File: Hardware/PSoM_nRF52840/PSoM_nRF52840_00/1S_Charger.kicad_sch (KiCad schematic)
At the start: 12 parts, among them U2 NPM1300-QEAA-R

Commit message: working on nrf52840
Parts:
- removed D201, D202: LED, LED_SMD:LED_0402_1005Metric, symbol Component_lib:LED
- removed R205, R206: 1k5, Resistor_SMD:R_0402_1005Metric, symbol Component_lib:R
- added C201, C205: 1u, symbol Component_lib:C
- added C202, C203, C204: 10u, symbol Component_lib:C
- added C206: 2u2, symbol Component_lib:C
- C207: renamed from C2; value C -> 10u
- C208: renamed from C3; value C -> 10u
- L201: renamed from L3; value L -> 2u2
- L202: renamed from L4; value L -> 2u2
- R203: renamed from R2; value 0 -> 47k
- renumbered R1 to R204, SHIPHLD to SHIPHLD1, U2 to U201
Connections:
- net BATTERY_TEMP: now also U201.18 (NTC)
- net GND: now also C207.2, C208.2, U201.2 (PVSS1), U201.28 (LSIN1/VINLDO1), U201.29 (LSOUT1/VOUTLDO1), U201.30 (LSIN2/VINLDO2), U201.31 (LSOUT2/VOUTLDO2), U201.6 (PVSS2), C201.1, C202.2, C203.2, C204.2, C205.2, C206.2
- net VBAT: now also U201.19 (VBAT), C206.1
- net VBUS: now also U201.21 (VBUS), C201.2
- net VSYS: now also U201.20 (VSYS), U201.4 (PVDD), C202.1, C203.1, C204.1
- net 3V3_EXT: now reaches L202.1
- net 3V3_EXT: now also C208.1, U201.32 (VOUT2)
- net SW2: now reaches L202.2
- net SW2: now also U201.5 (SW2)
- net 3V3_nRF: now reaches L201.1
- net 3V3_nRF: now also C207.1, U201.1 (VOUT1), U201.12 (VDDIO)
- net SW1: now reaches L201.2
- net SW1: now also U201.3 (SW1)
- net VBUS_OUT: now reaches U201.22 (VBUSOUT)
- net VBUS_OUT: now also C205.1
- net CC1: now reaches U201.23 (CC1)
- net CC2: now reaches U201.24 (CC2)
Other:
- note added: "200-1S Charger"
- note added: "VOUT1"
- note added: "VOUT2"
- note removed: "200- 1S Charger"
- moved on the sheet: C207, C208, L201, L202, R203, R204, SHIPHLD1, U201

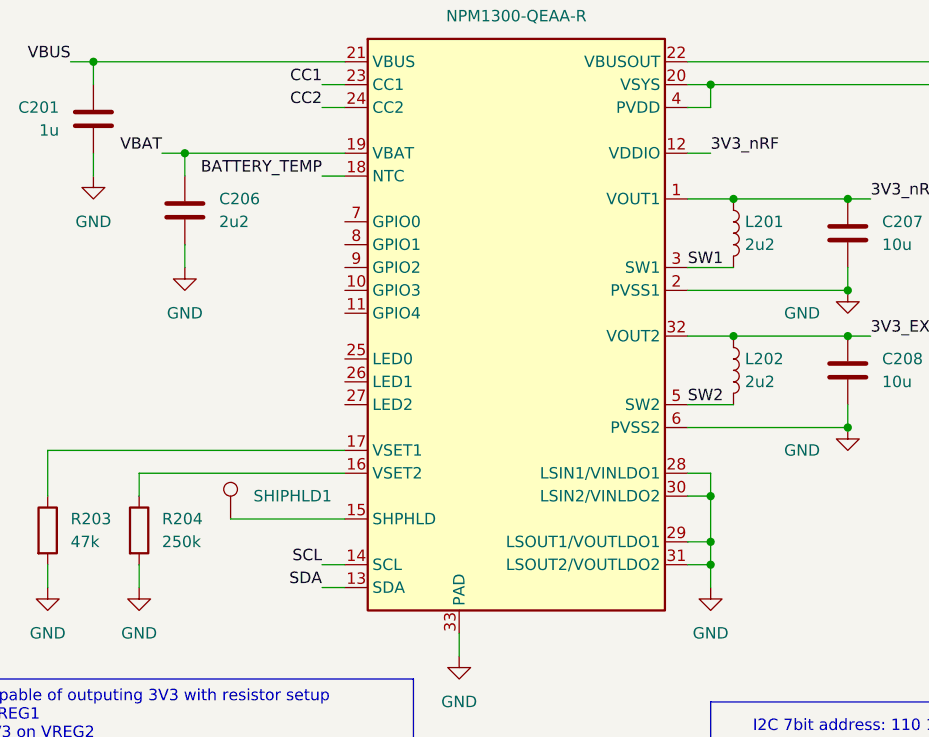
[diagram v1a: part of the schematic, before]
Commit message: footprint assignement done
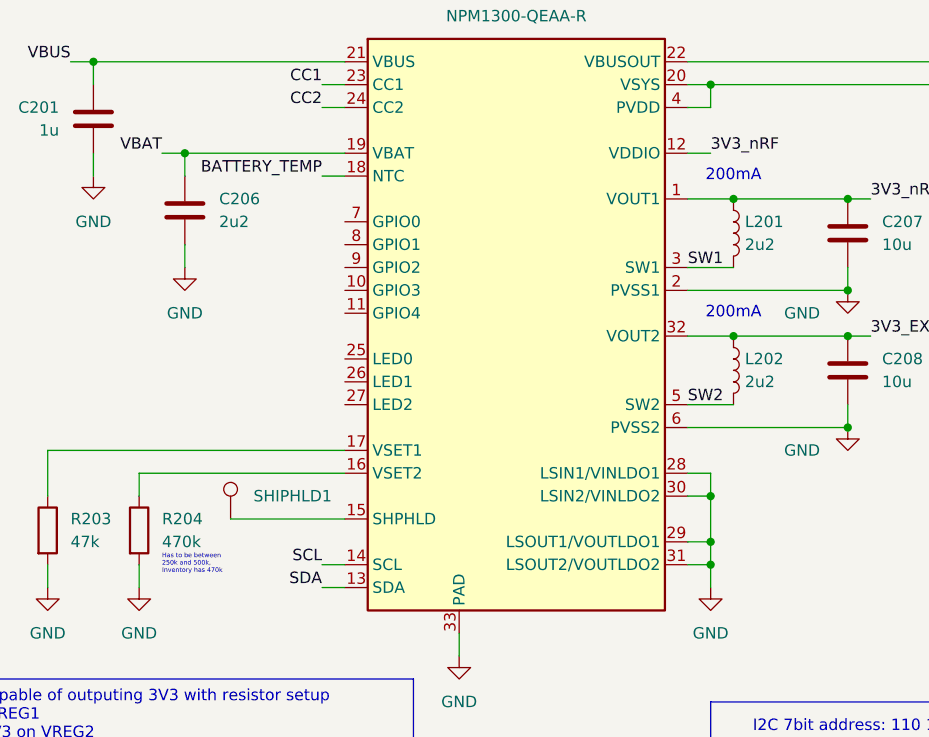
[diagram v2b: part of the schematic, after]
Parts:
- C201, C205, C207: footprint (none) -> Capacitor_SMD:C_0402_1005Metric
- C202, C203, C204, C206: footprint (none) -> Capacitor_SMD:C_0603_1608Metric
- C208: footprint (none) -> Capacitor_SMD:C_0402_1005Metric_Pad0.74x0.62mm_HandSolder
- L201, L202: footprint (none) -> Inductor_SMD:L_0603_1608Metric
- R203: footprint (none) -> Resistor_SMD:R_0201_0603Metric
- R204: value 250k -> 470k; footprint (none) -> Resistor_SMD:R_0201_0603Metric
- SHIPHLD1: footprint (none) -> TestPoint:TestPoint_Pad_D1.0mm
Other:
- note added: "200mA"
- note added: "Has to be between 250k and 500k, Inventory has 470k"
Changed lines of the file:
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@@
+		)
+	)
+	(text "200mA"
+		(exclude_from_sim no)
+		(at 167.64 81.28 0)
+		(effects
+			(font
+				(size 1.27 1.27)
+			)
+		)
+	)
+	(text "Has to be between\n250k and 500k,\nInventory has 470k"
+		(exclude_from_sim no)
+		(at 104.14 124.46 0)
+		(effects
+			(font
+				(size 0.508 0.508)
+			)
+			(justify left)
 		)
 	)
@@
 			(font
 				(face "Roboto")
+				(size 1.27 1.27)
+			)
+		)
+	)
+	(text "200mA"
+		(exclude_from_sim no)
+		(at 167.64 96.52 0)
+		(effects
+			(font
 				(size 1.27 1.27)
 			)
@@
 			)
 		)
-		(property "Footprint" ""
+		(property "Footprint" "Inductor_SMD:L_0603_1608Metric"
 			(at 167.64 102.87 90)
 			(effects
@@
 			)
 		)
-		(property "Footprint" ""
+		(property "Footprint" "Capacitor_SMD:C_0603_1608Metric"
 			(at 221.9452 81.28 0)
 			(effects
@@
 			)
 		)
-		(property "Footprint" ""
+		(property "Footprint" "Capacitor_SMD:C_0603_1608Metric"
 			(at 107.6452 88.9 0)
 			(effects
@@
 			)
 		)
-		(property "Footprint" ""
+		(property "Footprint" "Inductor_SMD:L_0603_1608Metric"
 			(at 167.64 87.63 90)
 			(effects
@@
 			)
 		)
-		(property "Footprint" ""
+		(property "Footprint" "Capacitor_SMD:C_0402_1005Metric"
 			(at 97.4852 71.12 0)
 			(effects
@@
 			)
 		)
-		(property "Footprint" ""
+		(property "Footprint" "Capacitor_SMD:C_0603_1608Metric"
 			(at 209.2452 81.28 0)
 			(effects
@@
 			)
 		)
-		(property "Footprint" ""
+		(property "Footprint" "TestPoint:TestPoint_Pad_D1.0mm"
 			(at 116.84 119.38 0)
 			(effects
@@
 			)
 		)
-		(property "Footprint" ""
+		(property "Footprint" "Resistor_SMD:R_0201_0603Metric"
 			(at 89.662 120.65 90)
 			(effects
@@
 			)
 		)
-		(property "Value" "250k"
+		(property "Value" "470k"
 			(at 104.14 121.9199 0)
 			(effects
@@
 			)
 		)
-		(property "Footprint" ""
+		(property "Footprint" "Resistor_SMD:R_0201_0603Metric"
 			(at 99.822 120.65 90)
 			(effects
@@
 			)
 		)
-		(property "Footprint" ""
+		(property "Footprint" "Capacitor_SMD:C_0402_1005Metric_Pad0.74x0.62mm_HandSolder"
 			(at 181.3052 106.68 0)
 			(effects
@@
 			)
 		)
-		(property "Footprint" ""
+		(property "Footprint" "Capacitor_SMD:C_0402_1005Metric"
 			(at 181.3052 91.44 0)
 			(effects
@@
 			)
 		)
-		(property "Footprint" ""
+		(property "Footprint" "Capacitor_SMD:C_0402_1005Metric"
 			(at 234.6452 78.74 0)
 			(effects
@@
 			)
 		)
-		(property "Footprint" ""
+		(property "Footprint" "Capacitor_SMD:C_0603_1608Metric"
 			(at 196.5452 81.28 0)
 			(effects

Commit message: working on schematic
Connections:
- net SHIP: now reaches SHIPHLD1.1, U201.15 (SHPHLD)
- net VSET2: now reaches R204.1, U201.16 (VSET2)
- net VSET1: now reaches R203.1, U201.17 (VSET1)
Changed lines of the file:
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@@
+		)
+	)
+	(label "VSET1"
+		(at 106.68 111.76 0)
+		(fields_autoplaced yes)
+		(effects
+			(font
+				(size 1.27 1.27)
+			)
+			(justify left bottom)
 		)
 	)
@@
 		)
 	)
+	(label "VSET2"
+		(at 106.68 114.3 0)
+		(fields_autoplaced yes)
+		(effects
+			(font
+				(size 1.27 1.27)
+			)
+			(justify left bottom)
+		)
+	)
 	(label "SCL"
 		(at 121.92 124.46 180)
@@
 		)
 	)
+	(label "SHIP"
+		(at 114.3 119.38 0)
+		(fields_autoplaced yes)
+		(effects
+			(font
+				(size 1.27 1.27)
+			)
+			(justify left bottom)
+		)
+	)

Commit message: routing is doing great progress
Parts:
- added D201, D202, D203: LED, symbol Component_lib:LED
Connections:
- net VSYS: now also D201.1 (A), D202.1 (A), D203.1 (A)
- net LED0: now reaches U201.25 (LED0)
- net LED0: now also D201.2 (K)
- net LED1: now reaches U201.26 (LED1)
- net LED1: now also D202.2 (K)
- net LED2: now reaches U201.27 (LED2)
- net LED2: now also D203.2 (K)
- no-connect marks 0 -> 5

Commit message: schematic should be done
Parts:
- D201, D202, D203: footprint (none) -> LED_SMD:LED_0402_1005Metric
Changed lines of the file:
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@@
+	(wire
+		(pts
+			(xy 266.7 73.66) (xy 269.24 73.66)
+		)
+		(stroke
+			(width 0)
+			(type default)
+		)
+	)
 	(wire
 		(pts
@@
 	(wire
 		(pts
-			(xy 269.24 68.58) (xy 266.7 68.58)
+			(xy 269.24 78.74) (xy 266.7 78.74)
 		)
 		(stroke
@@
 	(wire
 		(pts
-			(xy 266.7 68.58) (xy 266.7 71.12)
+			(xy 266.7 78.74) (xy 266.7 81.28)
 		)
 		(stroke
@@
 		(pts
 			(xy 55.88 86.36) (xy 55.88 88.9)
+		)
+		(stroke
+			(width 0)
+			(type default)
+		)
+	)
+	(wire
+		(pts
+			(xy 266.7 68.58) (xy 269.24 68.58)
 		)
 		(stroke
@@
 	(label "CC2"
 		(at 121.92 73.66 180)
+		(fields_autoplaced yes)
 		(effects
 			(font
@@
 	(label "VBAT"
 		(at 104.14 78.74 180)
+		(fields_autoplaced yes)
+		(effects
+			(font
+				(size 1.27 1.27)
+			)
+			(justify right bottom)
+		)
+	)
+	(label "SDA"
+		(at 266.7 73.66 180)
+		(fields_autoplaced yes)
 		(effects
 			(font
@@
 	(label "VSET1"
 		(at 106.68 111.76 0)
+		(fields_autoplaced yes)
 		(effects
 			(font
@@
 	(label "VBUS"
 		(at 93.98 68.58 180)
+		(fields_autoplaced yes)
 		(effects
 			(font
@@
 	(label "CC1"
 		(at 266.7 58.42 180)
+		(fields_autoplaced yes)
 		(effects
 			(font
@@
 	(label "CC2"
 		(at 266.7 63.5 180)
+		(fields_autoplaced yes)
 		(effects
 			(font
@@
 	(label "VBUS"
 		(at 266.7 27.94 180)
+		(fields_autoplaced yes)
 		(effects
 			(font
@@
 	(label "LED2"
 		(at 76.2 99.06 270)
+		(fields_autoplaced yes)
 		(effects
 			(font
@@
 	(label "BATTERY_TEMP"
 		(at 121.92 81.28 180)
+		(fields_autoplaced yes)
 		(effects
 			(font
@@
 	(label "VSYS"
 		(at 223.52 71.12 0)
+		(fields_autoplaced yes)
 		(effects
 			(font
@@
 	(label "VBUS_OUT"
 		(at 266.7 33.02 180)
+		(fields_autoplaced yes)
 		(effects
 			(font
@@
 	(label "LED1"
 		(at 66.04 99.06 270)
+		(fields_autoplaced yes)
 		(effects
 			(font
@@
 	(label "LED2"
 		(at 121.92 106.68 180)
+		(fields_autoplaced yes)
 		(effects
 			(font
@@
 	(label "LED0"
 		(at 121.92 101.6 180)
+		(fields_autoplaced yes)
 		(effects
 			(font
@@
 	(label "LED0"
 		(at 55.88 99.06 270)
+		(fields_autoplaced yes)
 		(effects
 			(font
@@
 	(label "3V3_nRF"
 		(at 182.88 83.82 0)
+		(fields_autoplaced yes)
 		(effects
 			(font
@@
 	(label "VBUS_OUT"
 		(at 236.22 68.58 0)
+		(fields_autoplaced yes)
 		(effects
 			(font
@@
 	(label "BATTERY_TEMP"
 		(at 266.7 43.18 180)
+		(fields_autoplaced yes)
 		(effects
 			(font
@@
 	(label "SW2"
 		(at 162.56 106.68 0)
+		(fields_autoplaced yes)
 		(effects
 			(font
@@
 	(label "SW1"
 		(at 162.56 91.44 0)
+		(fields_autoplaced yes)
 		(effects
 			(font
@@
 	(label "CC1"
 		(at 121.92 71.12 180)
+		(fields_autoplaced yes)
 		(effects
 			(font
@@
 	(label "3V3_nRF"
 		(at 165.1 78.74 0)
+		(fields_autoplaced yes)
 		(effects
 			(font
@@
 			)
 			(justify left bottom)
+		)
+	)
+	(label "SCL"
+		(at 266.7 68.58 180)
+		(fields_autoplaced yes)
+		(effects
+			(font
+				(size 1.27 1.27)
+			)
+			(justify right bottom)
 		)
 	)
 	(label "3V3_nRF"
 		(at 266.7 48.26 180)
+		(fields_autoplaced yes)
 		(effects
 			(font
@@
 	(label "3V3_EXT"
 		(at 182.88 99.06 0)
+		(fields_autoplaced yes)
 		(effects
 			(font
@@
 	(label "3V3_EXT"
 		(at 266.7 53.34 180)
+		(fields_autoplaced yes)
 		(effects
 			(font
@@
 	(label "VSYS"
 		(at 66.04 83.82 0)
+		(fields_autoplaced yes)
 		(effects
 			(font
@@
 	(label "VBAT"
 		(at 266.7 38.1 180)
+		(fields_autoplaced yes)
 		(effects
 			(font
@@
 	(label "LED1"
 		(at 121.92 104.14 180)
+		(fields_autoplaced yes)
 		(effects
 			(font
@@
 	(label "SDA"
 		(at 121.92 127 180)
+		(fields_autoplaced yes)
 		(effects
 			(font
@@
 	(label "VSET2"
 		(at 106.68 114.3 0)
+		(fields_autoplaced yes)
 		(effects
 			(font
@@
 	(label "SCL"
 		(at 121.92 124.46 180)
+		(fields_autoplaced yes)
 		(effects
 			(font
@@
 	(label "SHIP"
 		(at 114.3 119.38 0)
+		(fields_autoplaced yes)
 		(effects
 			(font
@@
 	(label "VSYS"
 		(at 266.7 22.86 180)
+		(fields_autoplaced yes)
 		(effects
 			(font
@@
 		(shape input)
 		(at 269.24 43.18 0)
+		(fields_autoplaced yes)
 		(effects
 			(font
@@
 		(shape output)
 		(at 269.24 53.34 0)
+		(fields_autoplaced yes)
+		(effects
+			(font
+				(size 1.27 1.27)
+			)
+			(justify left)
+		)
+	)
+	(hierarchical_label "SCL"
+		(shape input)
+		(at 269.24 68.58 0)
+		(fields_autoplaced yes)
 		(effects
 			(font
@@
 		(shape bidirectional)
 		(at 269.24 38.1 0)
+		(fields_autoplaced yes)
 		(effects
 			(font
@@
 		(shape output)
 		(at 269.24 22.86 0)
+		(fields_autoplaced yes)
 		(effects
 			(font
@@
 		(shape output)
 		(at 269.24 48.26 0)
+		(fields_autoplaced yes)
 		(effects
 			(font
@@
 	(hierarchical_label "GND"
 		(shape passive)
-		(at 269.24 68.58 0)
+		(at 269.24 78.74 0)
+		(fields_autoplaced yes)
+		(effects
+			(font
+				(size 1.27 1.27)
+			)
+			(justify left)
+		)
+	)
+	(hierarchical_label "SDA"
+		(shape bidirectional)
+		(at 269.24 73.66 0)
+		(fields_autoplaced yes)
 		(effects
 			(font
@@
 		(shape output)
 		(at 269.24 33.02 0)
+		(fields_autoplaced yes)
 		(effects
 			(font
@@
 		(shape bidirectional)
 		(at 269.24 63.5 0)
+		(fields_autoplaced yes)
 		(effects
 			(font
@@
 		(shape bidirectional)
 		(at 269.24 58.42 0)
+		(fields_autoplaced yes)
 		(effects
 			(font
@@
 		(shape input)
 		(at 269.24 27.94 0)
+		(fields_autoplaced yes)
 		(effects
 			(font
@@
 			)
 		)
-		(property "Footprint" ""
+		(property "Footprint" "LED_SMD:LED_0402_1005Metric"
 			(at 76.2 92.71 0)
 			(effects
@@
 	(symbol
 		(lib_id "power:GND")
-		(at 266.7 71.12 0)
+		(at 266.7 81.28 0)
 		(unit 1)
 		(exclude_from_sim no)
@@
 		(fields_autoplaced yes)
 		(property "Reference" "#PWR0202"
-			(at 266.7 77.47 0)
+			(at 266.7 87.63 0)
 			(effects
 				(font
@@
 		)
 		(property "Value" "GND"
-			(at 266.7 75.5634 0)
+			(at 266.7 85.7234 0)
 			(effects
 				(font
@@
 		)
 		(property "Footprint" ""
-			(at 266.7 71.12 0)
+			(at 266.7 81.28 0)
 			(effects
 				(font
@@
 		)
 		(property "Datasheet" ""
-			(at 266.7 71.12 0)
+			(at 266.7 81.28 0)
 			(effects
 				(font
@@
 		)
 		(property "Description" ""
-			(at 266.7 71.12 0)
+			(at 266.7 81.28 0)
 			(effects
 				(font
@@
 			)
 		)
-		(property "Footprint" ""
+		(property "Footprint" "LED_SMD:LED_0402_1005Metric"
 			(at 55.88 92.71 0)
 			(effects
@@
 			)
 		)
-		(property "Footprint" ""
+		(property "Footprint" "LED_SMD:LED_0402_1005Metric"
 			(at 66.04 92.71 0)
 			(effects

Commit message: working on the routing
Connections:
- net 3V3_EXT: now also C207.1, L201.1, U201.1 (VOUT1); no longer C208.1, L202.1, U201.32 (VOUT2)
- net 3V3_nRF: now also C208.1, L202.1, U201.32 (VOUT2); no longer C207.1, L201.1, U201.1 (VOUT1)
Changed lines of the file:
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@@
 	)
 	(label "3V3_nRF"
-		(at 182.88 83.82 0)
+		(at 182.88 99.06 0)
 		(fields_autoplaced yes)
 		(effects
@@
 	)
 	(label "3V3_EXT"
-		(at 182.88 99.06 0)
+		(at 182.88 83.82 0)
 		(fields_autoplaced yes)
 		(effects
